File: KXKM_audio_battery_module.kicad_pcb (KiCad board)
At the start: 2 copper layers, 56.5 x 57.5 mm, 81 parts, among them J1 Conn_01x06, J10 Conn_01x02, J11 TEST_1P, J12 Audio-Jack-3, J2 TEST_1P, J3 mikroBUS_socket, J4 Conn_01x04, J5 Micro_SD_Card, J6 Conn_01x03, J7 Conn_01x04, J8 Conn_01x02, J9 Conn_01x05, P1 TC_SWD, Q1 DMN63D8LDW, Q2 DMN63D8LDW, Q3 DMN63D8LDW, SW1 SW_Push, SW2 SW_Push, SW3 SW_Push, SW4 SW_SP3T, U1 ESP32-WROOM, U2 SP3485CN, U3 MCP16331T-E/CH, U4 BTS50080-1TEA, U5 DC_DC_POL, U6 PCM5141, U7 STM32F030F4Px

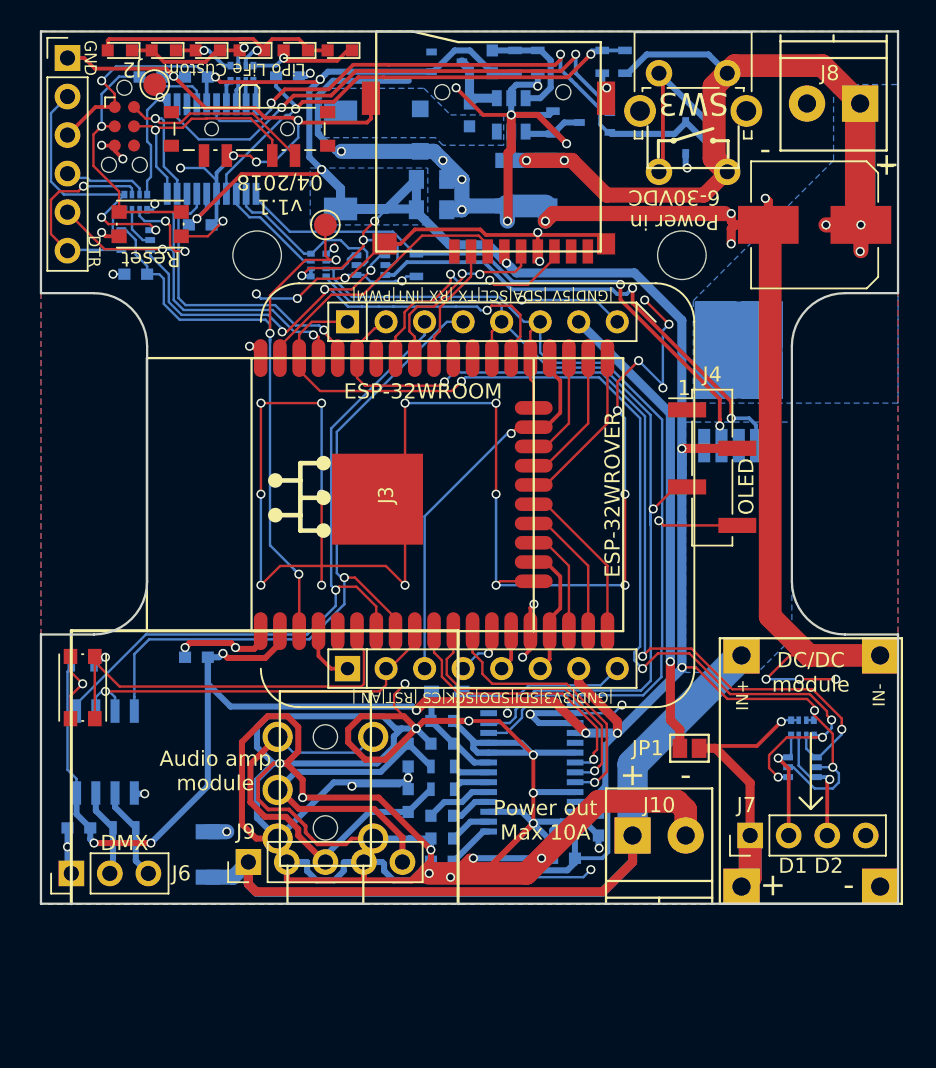
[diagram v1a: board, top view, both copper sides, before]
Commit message: v2.0 - audio circuitry on a separate board ; optimized connectors and lots of improvements
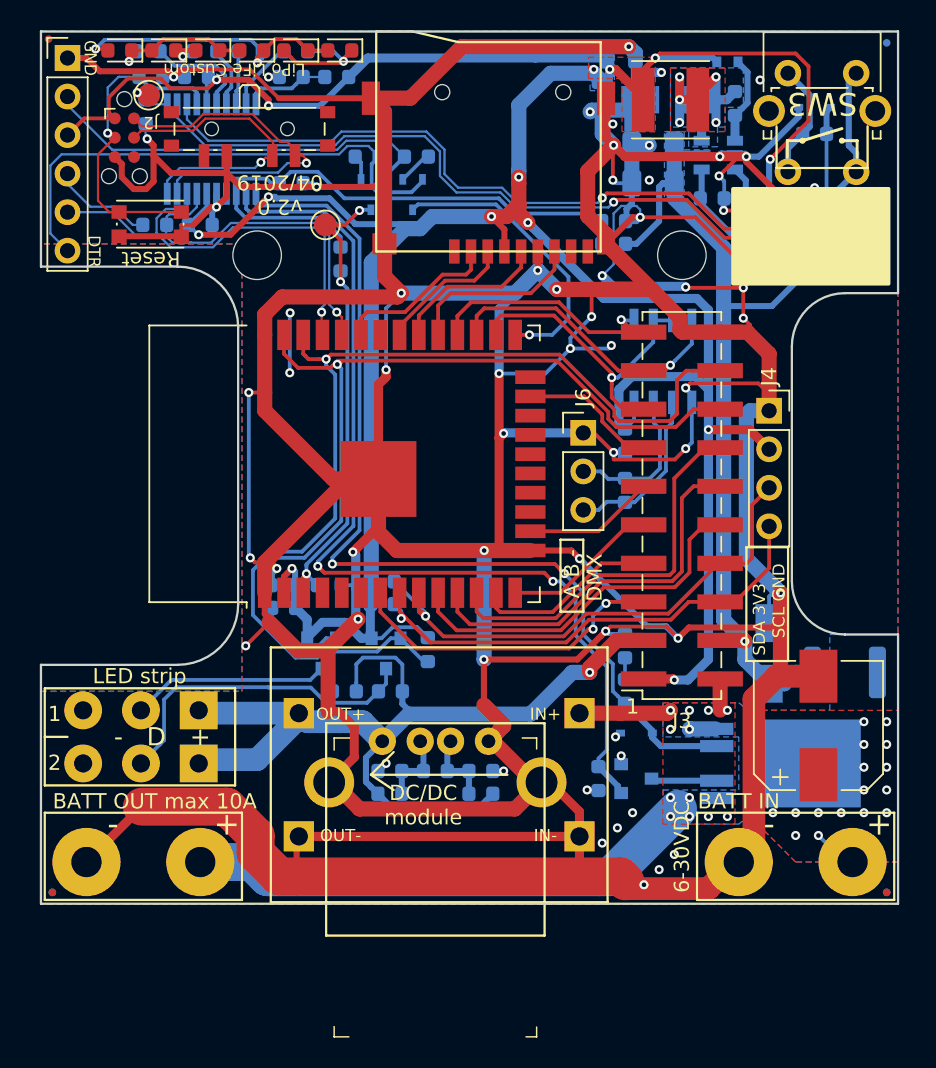
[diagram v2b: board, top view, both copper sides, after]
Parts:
- removed C11: 10uF,10V, Capacitors_SMD:C_0805
- removed C12: 1uF, Capacitors_SMD:C_0603
- removed C13, C14, C15, C18: 0.1uF, Capacitors_SMD:C_0603
- removed C16, C17: 2.2uF,25V, Capacitors_SMD:C_0603
- removed C19, C20: 2.2nF, Capacitors_SMD:C_0603
- removed C25: 10uF,50V, Capacitors_SMD:C_1206
- removed J10: Conn_01x02, Connectors_Terminal_Blocks:TerminalBlock_Pheonix_PT-3.5mm_2pol
- removed J12: Audio-Jack-3, tom_kicad_lib:Jack_3.5mm_stereo_PJ-313D
- removed JP1: Jumper_NO_Small, tom_kicad_lib:Solder_Jumper_2_open
- removed Q3: DMN63D8LDW, TO_SOT_Packages_SMD:SOT-363_SC-70-6
- removed RN1, RN3: 10k, Resistors_SMD:R_Array_Convex_4x0402
- removed RN2: 1k, Resistors_SMD:R_Array_Convex_4x0402
- removed RN4: 4*100R, Resistors_SMD:R_Array_Convex_4x0402
- removed SW2: SW_Push, Buttons_Switches_SMD:SW_SPST_KMR2
- removed U6: PCM5141, Housings_SSOP:TSSOP-28_4.4x9.7mm_Pitch0.65mm
- added C26: 10nF, Capacitor_SMD:C_0603_1608Metric, B.Cu at (147.2, 91.5)
- added D11: 100V,1A, Diode_SMD:D_SMA, B.Cu at (151.0, 121.5)
- added D12: 1N4148WT, Diode_SMD:D_SOD-523, B.Cu at (148.2, 82.5)
- added D13: Zener,3V,300mW, Diode_SMD:D_SOD-323, B.Cu at (142.2, 126.8)
- added F1: 30V,0.5A, Fuse:Fuse_1812_4532Metric, B.Cu at (156.0, 122.8)
- added FID1: Fiducial, Fiducial:Fiducial_0.5mm_Mask1mm, F.Cu at (103.8, 137.2)
- added FID2: Fiducial, Fiducial:Fiducial_0.5mm_Mask1mm, F.Cu at (158.8, 137.2)
- added FID3: Fiducial, Fiducial:Fiducial_0.5mm_Mask1mm, F.Cu at (103.5, 81.0)
- added FID4: Fiducial, Fiducial:Fiducial_0.5mm_Mask1mm, B.Cu at (158.8, 137.2)
- added FID5: Fiducial, Fiducial:Fiducial_0.5mm_Mask1mm, B.Cu at (103.8, 137.2)
- added FID6: Fiducial, Fiducial:Fiducial_0.5mm_Mask1mm, B.Cu at (158.8, 81.2)
- added J13: Wire pad, Connector_Wire:SolderWirePad_1x01_Drill2mm, F.Cu at (156.5, 135.2)
- added J14: Wire pad, Connector_Wire:SolderWirePad_1x01_Drill2mm, F.Cu at (149.0, 135.2)
- added J15: Wire pad, Connector_Wire:SolderWirePad_1x01_Drill2mm, F.Cu at (113.5, 135.2)
- added J16: Wire pad, Connector_Wire:SolderWirePad_1x01_Drill2mm, F.Cu at (106.0, 135.2)
- added Q4: 2N7002, Package_TO_SOT_SMD:SOT-23, B.Cu at (121.5, 121.5)
- added Q5: 2N7002, Package_TO_SOT_SMD:SOT-23, B.Cu at (125.8, 121.5)
- added Q6: 2N7002, Package_TO_SOT_SMD:SOT-23, B.Cu at (142.2, 129.8)
- added R11: 10k, Resistor_SMD:R_0603_1608Metric, B.Cu at (122.8, 95.5)
- added R17: 10k, Resistor_SMD:R_0603_1608Metric, B.Cu at (119.0, 118.5)
- added R18: 10k, Resistor_SMD:R_0603_1608Metric, B.Cu at (128.5, 121.2)
- added R19: 10k, Resistor_SMD:R_0603_1608Metric, B.Cu at (123.0, 124.0)
- added R20: 10k, Resistor_SMD:R_0603_1608Metric, B.Cu at (126.0, 124.0)
- added R21: 10k, Resistor_SMD:R_0603_1608Metric, B.Cu at (139.8, 129.8)
- added R22: 1k,1%, Resistor_SMD:R_0603_1608Metric, B.Cu at (141.5, 121.0)
- added R23: 1k, Resistor_SMD:R_0603_1608Metric, B.Cu at (109.9, 85.8)
- added R24: 100R, Resistor_SMD:R_0603_1608Metric, B.Cu at (119.8, 81.8)
- added R25: 100R, Resistor_SMD:R_0603_1608Metric, B.Cu at (116.8, 81.8)
- added R26: 100R, Resistor_SMD:R_0603_1608Metric, B.Cu at (110.1, 81.8)
- added R27: 100R, Resistor_SMD:R_0603_1608Metric, B.Cu at (113.8, 81.8)
- added R28: 10k,1%, Resistor_SMD:R_0603_1608Metric, B.Cu at (122.5, 83.5)
- added R29: DNP, Resistor_SMD:R_0603_1608Metric, B.Cu at (126.0, 130.8)
- added R3: 10k, Resistor_SMD:R_0603_1608Metric, B.Cu at (125.5, 118.2)
- added R30: DNP, Resistor_SMD:R_0603_1608Metric, B.Cu at (126.0, 129.2)
- added R31: 0R, Resistor_SMD:R_0603_1608Metric, B.Cu at (129.0, 129.2)
- added R4: 10k, Resistor_SMD:R_0603_1608Metric, B.Cu at (125.5, 116.8)
- added R5: 10k, Resistor_SMD:R_0603_1608Metric, B.Cu at (127.8, 88.8)
- added R6: 10k, Resistor_SMD:R_0603_1608Metric, B.Cu at (124.5, 88.8)
- added TH1: Thermistor_NTC, Resistor_SMD:R_0603_1608Metric, B.Cu at (119.5, 83.5)
- C1, C2, C22, C23, C24, C3, C7, C8: footprint Capacitors_SMD:C_0603 -> Capacitor_SMD:C_0603_1608Metric
- C10, C9: footprint Capacitors_SMD:C_0805 -> Capacitor_SMD:C_0805_2012Metric
- C21: value 2.2nF -> 1nF; footprint Capacitors_SMD:C_0603 -> Capacitor_SMD:C_0603_1608Metric
- C4, C5: footprint Capacitors_SMD:C_1206 -> Capacitor_SMD:C_1206_3216Metric
- C6: footprint Capacitors_SMD:CP_Elec_8x10 -> Capacitor_SMD:CP_Elec_8x10
- D1, D4: value BAT54CW -> 1N4148WT; footprint TO_SOT_Packages_SMD:SOT-323_SC-70 -> Diode_SMD:D_SOD-523
- D10, D5, D6, D7, D8, D9: footprint LEDs:LED_0603 -> LED_SMD:LED_0603_1608Metric
- D2: footprint Diodes_SMD:D_SOD-323 -> Diode_SMD:D_SOD-323
- D3: value 1A,60V -> 100V,1A; footprint Diodes_SMD:D_SOD-123F -> Diode_SMD:D_SMA
- J1: footprint Pin_Headers:Pin_Header_Straight_1x06_Pitch2.54mm -> Connector_PinHeader_2.54mm:PinHeader_1x06_P2.54mm_Vertical
- J11, J2: footprint Connectors_TestPoints:Test_Point_Pad_d1.5mm -> TestPoint:TestPoint_Pad_D1.5mm
- J3: value mikroBUS_socket -> Conn_02x10_Odd_Even; footprint MIKROBUS_HOST_CONN -> Connector_PinSocket_2.54mm:PinSocket_2x10_P2.54mm_Vertical_SMD
- J4: footprint Pin_Headers:Pin_Header_Straight_1x04_Pitch2.54mm_SMD_Pin1Left -> Connector_PinSocket_2.54mm:PinSocket_1x04_P2.54mm_Vertical
- J6: footprint Pin_Headers:Pin_Header_Straight_1x03_Pitch2.54mm -> Connector_PinHeader_2.54mm:PinHeader_1x03_P2.54mm_Vertical
- J7: value Conn_01x04 -> Conn_01x03; footprint Pin_Headers:Pin_Header_Straight_1x04_Pitch2.54mm -> tom_kicad_lib:SolderWirePad_1x03_P3.81mm_Drill1.2mm
- J8: value Conn_01x02 -> Conn_01x03; footprint Connectors_Terminal_Blocks:TerminalBlock_Pheonix_PT-3.5mm_2pol -> tom_kicad_lib:SolderWirePad_1x03_P3.81mm_Drill1.2mm
- J9: value Conn_01x05 -> USB_A; footprint Socket_Strips:Socket_Strip_Straight_1x05_Pitch2.54mm -> tom_kicad_lib:USB_A_Female
- L1: footprint Inductors_SMD:L_7.3x7.3_H4.5 -> Inductor_SMD:L_Taiyo-Yuden_NR-50xx; moved to F.Cu
- MK1, MK2: footprint Mounting_Holes:MountingHole_3.2mm_M3 -> MountingHole:MountingHole_3.2mm_M3
- P1: footprint Connectors:Tag-Connect_TC2030-IDC-NL -> Connector:Tag-Connect_TC2030-IDC-NL_2x03_P1.27mm_Vertical
- Q1, Q2: value DMN63D8LDW -> BC847W; footprint TO_SOT_Packages_SMD:SOT-363_SC-70-6 -> Package_TO_SOT_SMD:SOT-323_SC-70
- R1, R10, R15, R16, R7, R8, R9: footprint Resistors_SMD:R_0603 -> Resistor_SMD:R_0603_1608Metric
- R12: value 470R -> 1k,1%; footprint Resistors_SMD:R_0603 -> Resistor_SMD:R_0603_1608Metric
- R13, R14: value 470R -> DNP; footprint Resistors_SMD:R_0603 -> Resistor_SMD:R_0603_1608Metric
- R2: value 10k,1% -> 1k; footprint Resistors_SMD:R_0603 -> Resistor_SMD:R_0603_1608Metric
- SW1: footprint Buttons_Switches_SMD:SW_SPST_KMR2 -> Button_Switch_SMD:SW_SPST_KMR2
- SW4: footprint Buttons_Switches_SMD:SW_SP3T_PCM13 -> Button_Switch_SMD:SW_SP3T_PCM13
- U1: footprint tom_kicad_lib:ESP32-WROOM_WROVER -> RF_Module:ESP32-WROOM-32
- U2: footprint Housings_SOIC:SOIC-8_3.9x4.9mm_Pitch1.27mm -> Package_SO:SOIC-8_3.9x4.9mm_P1.27mm
- U3: footprint TO_SOT_Packages_SMD:SOT-23-6 -> Package_TO_SOT_SMD:SOT-23-6
- U4: footprint TO_SOT_Packages_SMD:TO-252-5_TabPin6 -> Package_TO_SOT_SMD:TO-252-4
- U5: footprint tom_kicad_lib:DC_DC_buck_module_Mini360 -> tom_kicad_lib:DC_DC_Buck_module_22x17mm
- U7: footprint Housings_SSOP:TSSOP-20_4.4x6.5mm_Pitch0.65mm -> Package_SO:TSSOP-20_4.4x6.5mm_P0.65mm
- moved J8 61.6 mm to (113.4, 128.8)
- moved Q2 47.3 mm to (124.8, 91.2), turned to 270 degrees
- moved U2 44.9 mm to (144.0, 102.2)
- moved J6 44.5 mm to (138.8, 107.0), turned to 0 degrees
- moved C3 44.1 mm to (141.5, 107.5), turned to 270 degrees
- moved R7 39.8 mm to (141.5, 110.8), turned to 90 degrees
- moved J7 37.3 mm to (113.4, 125.2), turned to 180 degrees
- moved C6 33.0 mm to (154.2, 126.2), turned to 90 degrees
- moved R12 31.3 mm to (141.5, 124.0)
- moved R2 29.4 mm to (110.5, 93.2), turned to 180 degrees
- moved D4 25.7 mm to (151.3, 96.5)
- moved U4 25.3 mm to (151.8, 128.8), turned to 0 degrees
- moved J3 24.5 mm to (145.2, 111.8), turned to 180 degrees
- moved U5 24.5 mm to (129.2, 129.5), turned to 180 degrees
- moved C1 24.1 mm to (122.0, 117.0), turned to 0 degrees
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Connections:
- C6 pad 1: +BATT -> +BATT_RAW
- D1 pad 1: /Battery monitoring/3.3V_EN -> Net-(C26-Pad1)
- D1 pad 2: /Battery monitoring/EN_PUSH_BUTTON -> /Battery monitoring/3.3V_EN
- D4 pad 1: +3V3 -> Net-(C26-Pad1)
- D4 pad 2: Net-(D4-Pad2) -> /Battery monitoring/EN_PUSH_BUTTON
- J3 pad 1: /ADC_IN -> +3V3
- J3 pad 10: +5V -> /I2S_LRCK
- J3 pad 11: /I2C_SDA -> /SPI_MOSI
- J3 pad 12: /I2C_SCL -> /I2S_DATA
- J3 pad 13: /DMX_DI -> /SPI_CS
- J3 pad 14: /DMX_RO -> /I2S_BCK
- J3 pad 15: /LED_DATA_1 -> /DMX_DE
- J3 pad 16: /LED_DATA_2 -> /LED_DATA_1
- J3 pad 2: /DMX_DE -> +VSW
- J3 pad 3: /SPI_CS -> VBUS
- J3 pad 4: /SPI_SCK -> +BATT
- J3 pad 5: /SPI_MISO -> /ADC_IN
- J3 pad 6: /SPI_MOSI -> /I2C_SDA
- J3 pad 7: +3V3 -> /SPI_SCK
- J3 pad 8: GND -> /I2C_SCL
- J3 pad 9: GND -> /SPI_MISO
- J7 pad 3: /LED_DATA_OUT_2 -> GND
- J8 pad 1: +BATT -> VBUS
- J8 pad 2: GND -> /LED_DATA_OUT_2
- J9 pad 1: +VSW -> VBUS
- J9 pad 2: GND -> Net-(J9-Pad2)
- J9 pad 3: /Audio/AUDIO_L -> Net-(J9-Pad3)
- J9 pad 5: /Audio/AUDIO_R -> GND
- Q1 pad 1: /PROG_DTR -> Net-(Q1-Pad1)
- Q1 pad 2: Net-(Q1-Pad2) -> /PROG_DTR
- Q1 pad 3: /ESP32_EN -> /ESP32_BOOT
- Q2 pad 1: /LED_DATA_2 -> Net-(Q2-Pad1)
- Q2 pad 2: +3V3 -> /PROG_RTS
- Q2 pad 3: /LED_DATA_OUT_1 -> /ESP32_EN
- R1 pad 1: Net-(D1-Pad3) -> Net-(C26-Pad1)
- R12 pad 1: /Battery monitoring/LOAD_I_SENSE -> Net-(R12-Pad1)
- R12 pad 2: GND -> /Battery monitoring/LOAD_I_SENSE
- R13 pad 1: /Audio/AUDIO_L -> VBUS
- R13 pad 2: Net-(R13-Pad2) -> Net-(J9-Pad3)
- R14 pad 1: /Audio/AUDIO_R -> Net-(J9-Pad3)
- R14 pad 2: Net-(R14-Pad2) -> GND
- R2 pad 1: +3V3 -> /ESP32_RXI
- R2 pad 2: /GP_PUSH_BTN -> Net-(J1-Pad4)
- SW3 pad : GND -> (no net)
- U1 pad 10: /I2S_BCK -> /I2S_LRCK
- U1 pad 12: /I2S_LRCK -> /I2S_BCK
- U1 pad 24: /I2C_SDA -> Net-(U1-Pad24)
- U1 pad 26: /I2C_SCL -> /DMX_DE
- U1 pad 27: Net-(U1-Pad27) -> /DMX_DI
- U1 pad 28: Net-(U1-Pad28) -> /DMX_RO
- U1 pad 29: /SD_CS -> /SD_DO
- U1 pad 31: /SD_DO -> /SD_DI
- U1 pad 33: /LED_DATA_1 -> /SD_CS
- U1 pad 37: /SD_DI -> /LED_DATA_1
- U1 pad 4: /ADC_IN -> Net-(U1-Pad4)
- U1 pad 6: /GP_PUSH_BTN -> Net-(U1-Pad6)
- U1 pad 7: /DMX_RO -> /ADC_IN
- U1 pad 8: /DMX_DI -> /I2C_SDA
- U1 pad 9: /DMX_DE -> /I2C_SCL
- U3 pad 4: Net-(D1-Pad3) -> Net-(C26-Pad1)
- U4 pad 3: (no net) -> +BATT_RAW
- U7 pad 10: /Battery monitoring/LED_BAR_1 -> /Battery monitoring/TEMP_MEAS
- U7 pad 3: Net-(U7-Pad3) -> /Battery monitoring/EN_PUSH_BUTTON
- U7 pad 6: /Battery monitoring/EN_PUSH_BUTTON -> /Battery monitoring/LED_BAR_3
- U7 pad 8: /Battery monitoring/LED_BAR_3 -> /Battery monitoring/LED_BAR_2
- U7 pad 9: /Battery monitoring/LED_BAR_2 -> /Battery monitoring/LED_BAR_1
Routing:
- net /Battery monitoring/MAIN_OUT_EN: track 12.2 -> 63.9 mm, vias 0 -> 2
- net +3V3: track 276.8 -> 226.4 mm, vias 19 -> 14
- net VBUS: track 22.3 -> 62.4 mm
- net /I2C_SDA: track 71.8 -> 32.7 mm
- net +VSW: track 77.1 -> 44.1 mm, vias 0 -> 12
- net +5V: track 30.9 -> 0.00 mm, vias 1 -> 0
- net /DMX_RO: track 46.6 -> 17.4 mm
- net /GP_PUSH_BTN: track 28.4 -> 0.00 mm, vias 1 -> 0
- net /Audio/AUDIO_L: track 28.2 -> 0.00 mm
- net Net-(Q6-Pad3): track 32.1 -> 4.36 mm, vias 2 -> 0
- net /DMX_DI: track 47.3 -> 19.6 mm
- net /I2C_SCL: track 62.3 -> 34.8 mm
- net /Battery monitoring/LOAD_I_SENSE: track 40.1 -> 63.9 mm
- net /Audio/AUDIO_R: track 23.2 -> 0.00 mm
- net /PROG_DTR: track 13.6 -> 34.7 mm, vias 1 -> 0
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- added copper zone on F.Cu, net +3V3
- added copper zone on B.Cu, net +BATT_RAW
- added copper zone on F.Cu, net +BATT_RAW
- added copper zone on F.Cu, net +VSW
- added copper zone on F.Cu, net Net-(C7-Pad2)
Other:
- outline, holes or cut-outs redrawn
- net class Default: clearance 0.16 -> 0.15; trace_width 0.16 -> 0.15; via_drill 0.4 -> 0.3
- rule trace_clearance: 0.16 -> 0.15
- rule trace_min: 0.16 -> 0.15
- rule via_min_size: 0.4 -> 0.6
- board text added: "+ D -"
- board text added: "- D +"
- board text added: "1 2"
- board text added: "6-30VDC"
- board text added: "A B -"
- board text added: "BATT IN"
- board text added: "BATT OUT max 10A"
- board text added: "IN"
- board text added: "KXKM ESP32 battery management board"
- board text added: "LED strip"
- board text added: "OUT"
- board text added: "SDA 3V3 SCL GND"
- board text added: "T. Magnier - v2.0 - 04/2019"
- board text added: "v2.0 04/2019"
- board text removed: "+ -"
- board text removed: "36/AN 33/RST 15/CS 14/SCK 12/MISO 13/MOSI +3.3V GND"
- board text removed: "Audio amp module"
- board text removed: "D+ D- GND"
- board text removed: "D1 D2"
- board text removed: "For +5V close JP1"
- board text removed: "J2"
- board text removed: "KXKM ESP32 Audio & Battery"
- board text removed: "OLED"
- board text removed: "PWM/22 INT/21 RX/35 TX/32 SCL/4 SDA/2 +5V GND"
- board text removed: "Power in 6-30VDC"
- board text removed: "Power out Max 10A"
- board text removed: "R GND L GND VCC"
- board text removed: "Tom Magnier v1.1 04/2018"
- board text removed: "mikroBUS"
- board text removed: "v1.1 04/2018"
- board text removed: "|GND|3V3|SDI|SDO|SCK|CS |RST|AN |"
- board text removed: "|GND|5V |SDA|SCL|TX |RX |INT|PWM|"
